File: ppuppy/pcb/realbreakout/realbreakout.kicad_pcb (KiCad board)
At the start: 2 copper layers, 103.9 x 85.3 mm, 6 parts, among them J1 Conn_01x36, J2 Conn_01x36, J3 Conn_01x36, U1 nescartheader, U2 piheader

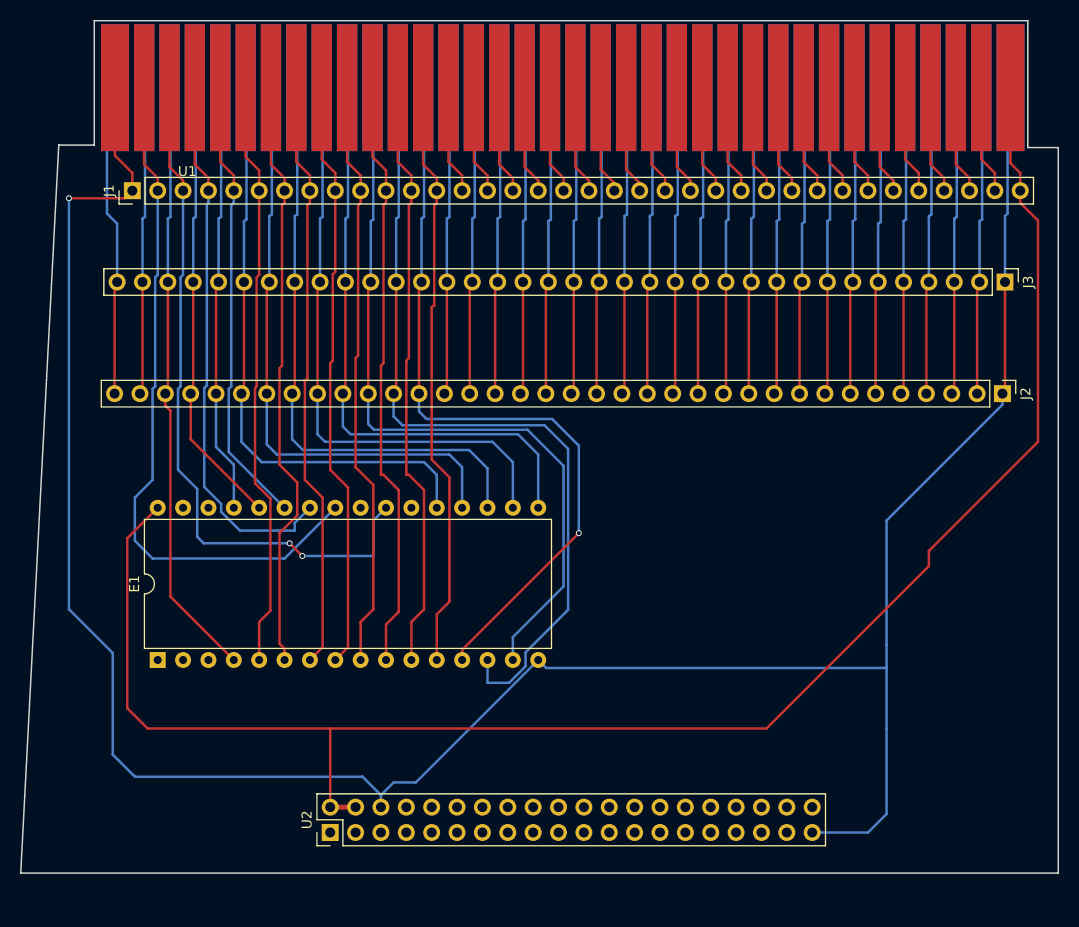
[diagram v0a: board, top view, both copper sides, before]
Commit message: More notes, work on breakout; add gpio 'direct access' code that is supposedly faster than bcm lib (but actually it appears to use the same approach, maybe without memory barrier)?
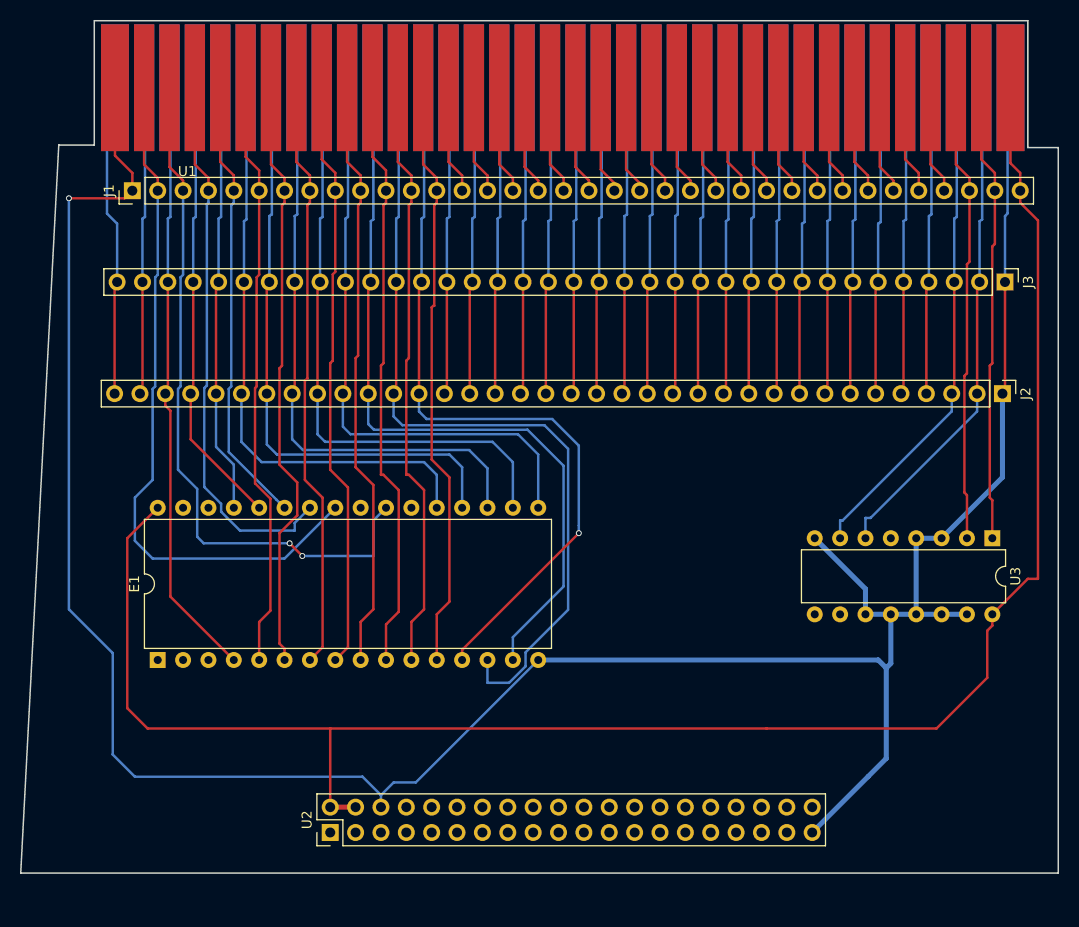
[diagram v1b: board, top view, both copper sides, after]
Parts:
- added U3: nescic, Housings_DIP:DIP-16_W7.62mm, F.Cu at (128.5, 88.9)
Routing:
- net Net-(J1-Pad34): track 10.9 -> 46.0 mm
- net Net-(J1-Pad35): track 10.9 -> 46.0 mm
- net Net-(J2-Pad2): track 30.9 -> 50.3 mm
- net Net-(J2-Pad3): track 30.9 -> 50.1 mm
- net GND: track 247.6 -> 265.7 mm
- net 5V: track 173.2 -> 183.7 mm

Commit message: sync rivercity
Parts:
- added G***: LOGO, footprints:logo, F.Cu at (124.1, 112.1)
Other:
- board size 103.9 x 85.3 mm -> 100.3 x 84.8 mm

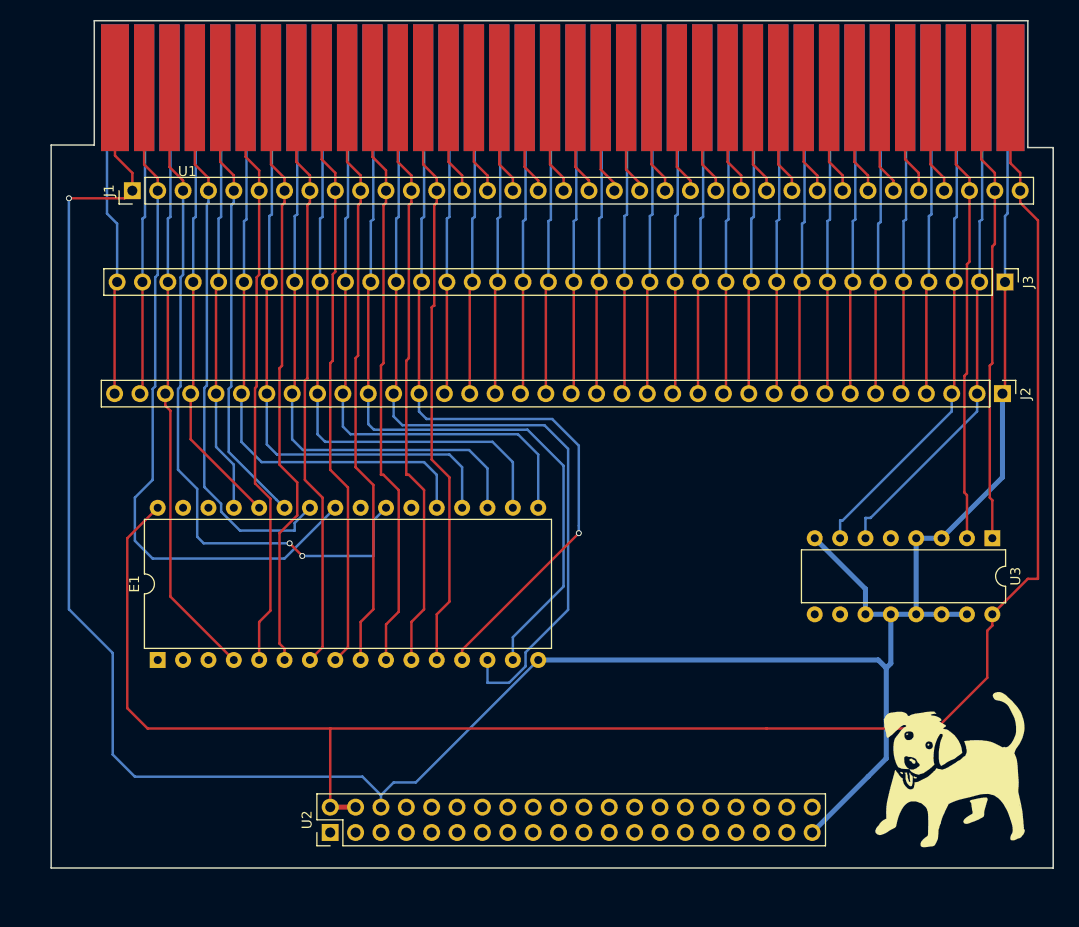
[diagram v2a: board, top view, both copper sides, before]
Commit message: Almost ready PCB, longer lead-in in cart knock
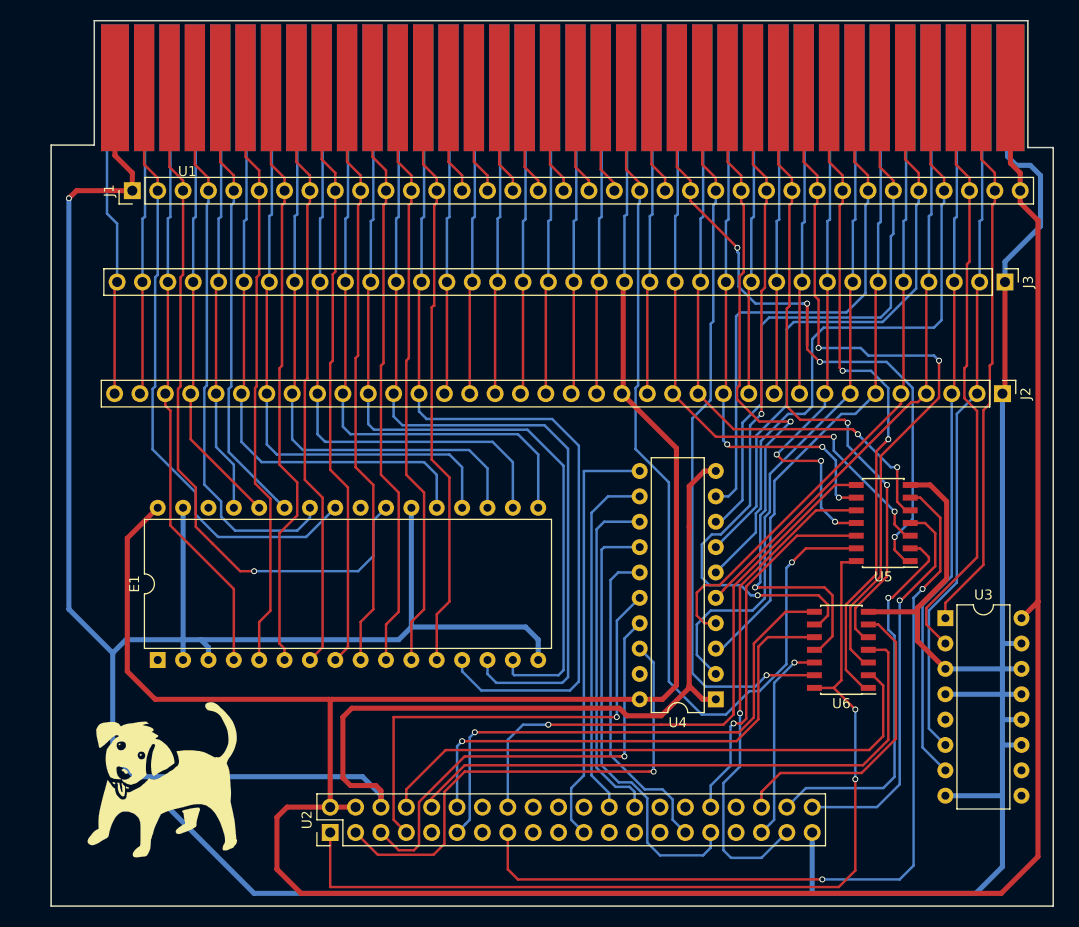
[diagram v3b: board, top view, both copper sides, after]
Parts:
- added U4: CD74FCT245, Housings_DIP:DIP-20_W7.62mm, F.Cu at (100.8, 105.0)
- added U5: MC74VHCT50A, Housings_SOIC:SOIC-14_3.9x8.7mm_Pitch1.27mm, F.Cu at (117.6, 87.4)
- added U6: MC74VHCT50A, Housings_SOIC:SOIC-14_3.9x8.7mm_Pitch1.27mm, F.Cu at (113.4, 100.1)
- moved G*** 78.9 mm to (45.2, 113.2)
- moved U3 9.28 mm to (123.8, 96.9), turned to 0 degrees
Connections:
- E1 pad 2: (no net) -> GND
- E1 pad 22: (no net) -> GND
- E1 pad 24: (no net) -> Net-(E1-Pad24)
- E1 pad 3: (no net) -> GND
- E1 pad 31: (no net) -> GND
- J2 pad 16: Net-(J2-Pad16) -> 5V
- J2 pad 23: Net-(J2-Pad23) -> Net-(E1-Pad24)
- J3 pad 16: Net-(J2-Pad16) -> 5V
- J3 pad 23: Net-(J2-Pad23) -> Net-(E1-Pad24)
- U1 pad 50: Net-(J2-Pad23) -> Net-(E1-Pad24)
- U1 pad 57: Net-(J2-Pad16) -> 5V
- U2 pad 1: (no net) -> 3v
- U2 pad 10: (no net) -> 3vA1
- U2 pad 11: (no net) -> 3vA3
- U2 pad 12: (no net) -> 3vA4
- U2 pad 15: (no net) -> 3vA8
- U2 pad 16: (no net) -> 3vA9
- U2 pad 21: (no net) -> Net-(U2-Pad21)
- U2 pad 24: (no net) -> Net-(U2-Pad24)
- U2 pad 26: (no net) -> Net-(U2-Pad26)
- U2 pad 29: (no net) -> Net-(U2-Pad29)
- U2 pad 3: (no net) -> Net-(U2-Pad3)
- U2 pad 31: (no net) -> Net-(U2-Pad31)
- U2 pad 32: (no net) -> 3vRD
- U2 pad 35: (no net) -> 3vA5
- U2 pad 36: (no net) -> 3vA2
- U2 pad 37: (no net) -> 3vA13
- U2 pad 38: (no net) -> 3vA6
- U2 pad 40: (no net) -> 3vA7
- U2 pad 5: (no net) -> Net-(U2-Pad5)
- U2 pad 7: (no net) -> Net-(U2-Pad7)
- U2 pad 8: (no net) -> 3vA0
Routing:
- net GND: track 265.7 -> 492.0 mm
- net 5V: track 183.7 -> 319.9 mm
- net 3v: track 0.00 -> 94.3 mm, vias 0 -> 2
- net 3vA8: track 0.00 -> 85.1 mm, vias 0 -> 2
- net Net-(J1-Pad21): track 10.9 -> 94.3 mm, vias 0 -> 1
- net Net-(J1-Pad28): track 10.9 -> 74.4 mm, vias 0 -> 2
- net Net-(J1-Pad24): track 10.9 -> 73.4 mm, vias 0 -> 1
- net Net-(J1-Pad25): track 10.9 -> 71.1 mm, vias 0 -> 2
- net 3vA9: track 0.00 -> 60.1 mm, vias 0 -> 1
- net 3vA1: track 0.00 -> 59.9 mm
- net Net-(J1-Pad23): track 10.9 -> 70.0 mm, vias 0 -> 4
- net 3vA0: track 0.00 -> 58.7 mm
- net Net-(J1-Pad26): track 10.9 -> 69.4 mm, vias 0 -> 2
- net Net-(J1-Pad29): track 10.9 -> 67.4 mm, vias 0 -> 2
- net Net-(J1-Pad33): track 10.9 -> 66.0 mm
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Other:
- board size 100.3 x 84.8 mm -> 100.3 x 88.6 mm
- net class Thick added: clearance 0.254, trace_width 0.508, via_dia 0.6, via_drill 0.4

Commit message: This is the version of PCB that I first printed
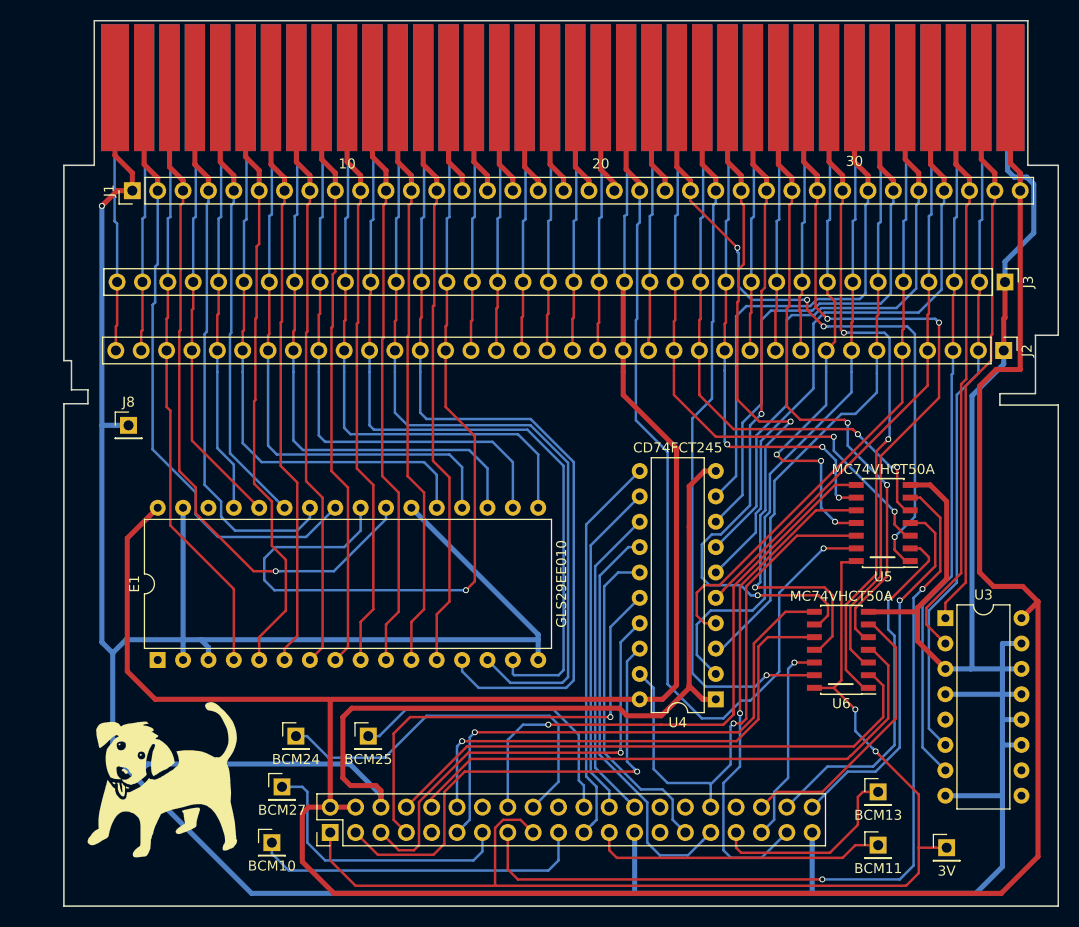
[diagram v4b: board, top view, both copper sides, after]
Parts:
- added J10: BCM11, Pin_Headers:Pin_Header_Straight_1x01_Pitch2.54mm, F.Cu at (117.1, 119.6)
- added J11: BCM13, Pin_Headers:Pin_Header_Straight_1x01_Pitch2.54mm, F.Cu at (117.1, 114.3)
- added J4: BCM25, Pin_Headers:Pin_Header_Straight_1x01_Pitch2.54mm, F.Cu at (66.0, 108.7)
- added J5: BCM24, Pin_Headers:Pin_Header_Straight_1x01_Pitch2.54mm, F.Cu at (58.8, 108.7)
- added J6: BCM27, Pin_Headers:Pin_Header_Straight_1x01_Pitch2.54mm, F.Cu at (57.4, 113.8)
- added J7: 3V, Pin_Headers:Pin_Header_Straight_1x01_Pitch2.54mm, F.Cu at (124.0, 119.9)
- added J8: GND, Pin_Headers:Pin_Header_Straight_1x01_Pitch2.54mm, F.Cu at (42.0, 77.6)
- added J9: BCM10, Pin_Headers:Pin_Header_Straight_1x01_Pitch2.54mm, F.Cu at (56.4, 119.4)
- moved J2 4.32 mm to (129.7, 70.1)
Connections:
- net Net-(E1-Pad24) renamed /ROMSEL
- net Net-(J1-Pad21) renamed /5vRD
- U2 pad 13: (no net) -> Net-(J6-Pad1)
- U2 pad 17: (no net) -> 3v
- U2 pad 18: (no net) -> Net-(J5-Pad1)
- U2 pad 19: (no net) -> Net-(J9-Pad1)
- U2 pad 22: (no net) -> Net-(J4-Pad1)
- U2 pad 23: (no net) -> Net-(J10-Pad1)
- U2 pad 25: (no net) -> GND
- U2 pad 33: (no net) -> Net-(J11-Pad1)
- U4 pad 19: (no net) -> 3vRD
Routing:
- net /ROMSEL: track 30.9 -> 88.0 mm, vias 0 -> 1
- net Net-(J5-Pad1): track 0.00 -> 38.6 mm
- net Net-(J9-Pad1): track 0.00 -> 33.7 mm
- net Net-(J4-Pad1): track 0.00 -> 30.7 mm
- net Net-(J10-Pad1): track 0.00 -> 29.5 mm
- net Net-(J6-Pad1): track 0.00 -> 28.4 mm
- net 3v: track 94.3 -> 115.0 mm
- net Net-(J11-Pad1): track 0.00 -> 20.1 mm
- net 3vRD: track 37.2 -> 53.6 mm
- net GND: track 492.0 -> 505.4 mm
- net Net-(J2-Pad36): track 31.5 -> 26.8 mm
- net Net-(J2-Pad20): track 30.9 -> 26.5 mm
- net Net-(J2-Pad35): track 30.9 -> 26.5 mm
- net Net-(J2-Pad18): track 30.9 -> 26.5 mm
- net Net-(J2-Pad10): track 30.9 -> 26.5 mm
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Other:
- board size 100.3 x 88.6 mm -> 99.6 x 88.6 mm
- board text added: "3600mils"
- board text added: "3680"

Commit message: I measured this wrong. Fix it
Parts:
- moved U1 0.79 mm to (38.2, 50.1)

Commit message: v2 of board
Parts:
- added .1uf1: .1uf, Capacitors_THT:C_Disc_D5.0mm_W2.5mm_P5.00mm, F.Cu at (99.5, 108.3)
- added .1uf2: .1uf, Capacitors_THT:C_Disc_D5.0mm_W2.5mm_P5.00mm, F.Cu at (119.0, 93.6)
- added .1uf3: .1uf, Capacitors_THT:C_Disc_D5.0mm_W2.5mm_P5.00mm, F.Cu at (121.7, 80.8)
- added J12: /OE, Pin_Headers:Pin_Header_Straight_1x01_Pitch2.54mm, F.Cu at (94.4, 78.4)
- added REF**: MountingHole_6.5mm, Mounting_Holes:MountingHole_6.5mm, F.Cu at (85.9, 104.4)
- moved E1 6.06 mm to (41.7, 96.0)
- moved J8 2.41 mm to (42.0, 75.2)
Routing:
- net GND: track 505.4 -> 436.8 mm
- net /5vRD: track 93.7 -> 61.3 mm, vias 1 -> 2
- net 3vRD: track 53.6 -> 74.5 mm, vias 1 -> 2
- net /ROMSEL: track 88.0 -> 68.4 mm
- net 3vA9: track 60.1 -> 74.4 mm
- net Net-(U2-Pad26): track 32.1 -> 45.0 mm
- net Net-(E1-Pad15): track 82.7 -> 69.7 mm
- net Net-(U2-Pad31): track 41.7 -> 54.6 mm
- net Net-(E1-Pad13): track 85.7 -> 72.9 mm
- net Net-(U2-Pad24): track 33.9 -> 45.8 mm
- net Net-(E1-Pad14): track 82.9 -> 71.0 mm
- net Net-(U2-Pad21): track 39.4 -> 51.2 mm
- net Net-(E1-Pad20): track 60.8 -> 49.7 mm
- net Net-(E1-Pad18): track 60.5 -> 49.9 mm
- net Net-(E1-Pad19): track 60.1 -> 49.7 mm
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- added copper zone on B.Cu, net GND
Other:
- outline, holes or cut-outs redrawn
- board text added: "/RD"
- board text added: "2018"
- board text added: "5V"
- board text added: "@tom7"
- board text added: "GND"
- board text added: "v2!"
